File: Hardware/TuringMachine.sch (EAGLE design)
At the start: 78 parts, among them IC1 TL072P, IC2 4015, IC3 4015, IC5 4016, IC6 TL072P, IC7 TL072P, T1 2N3904

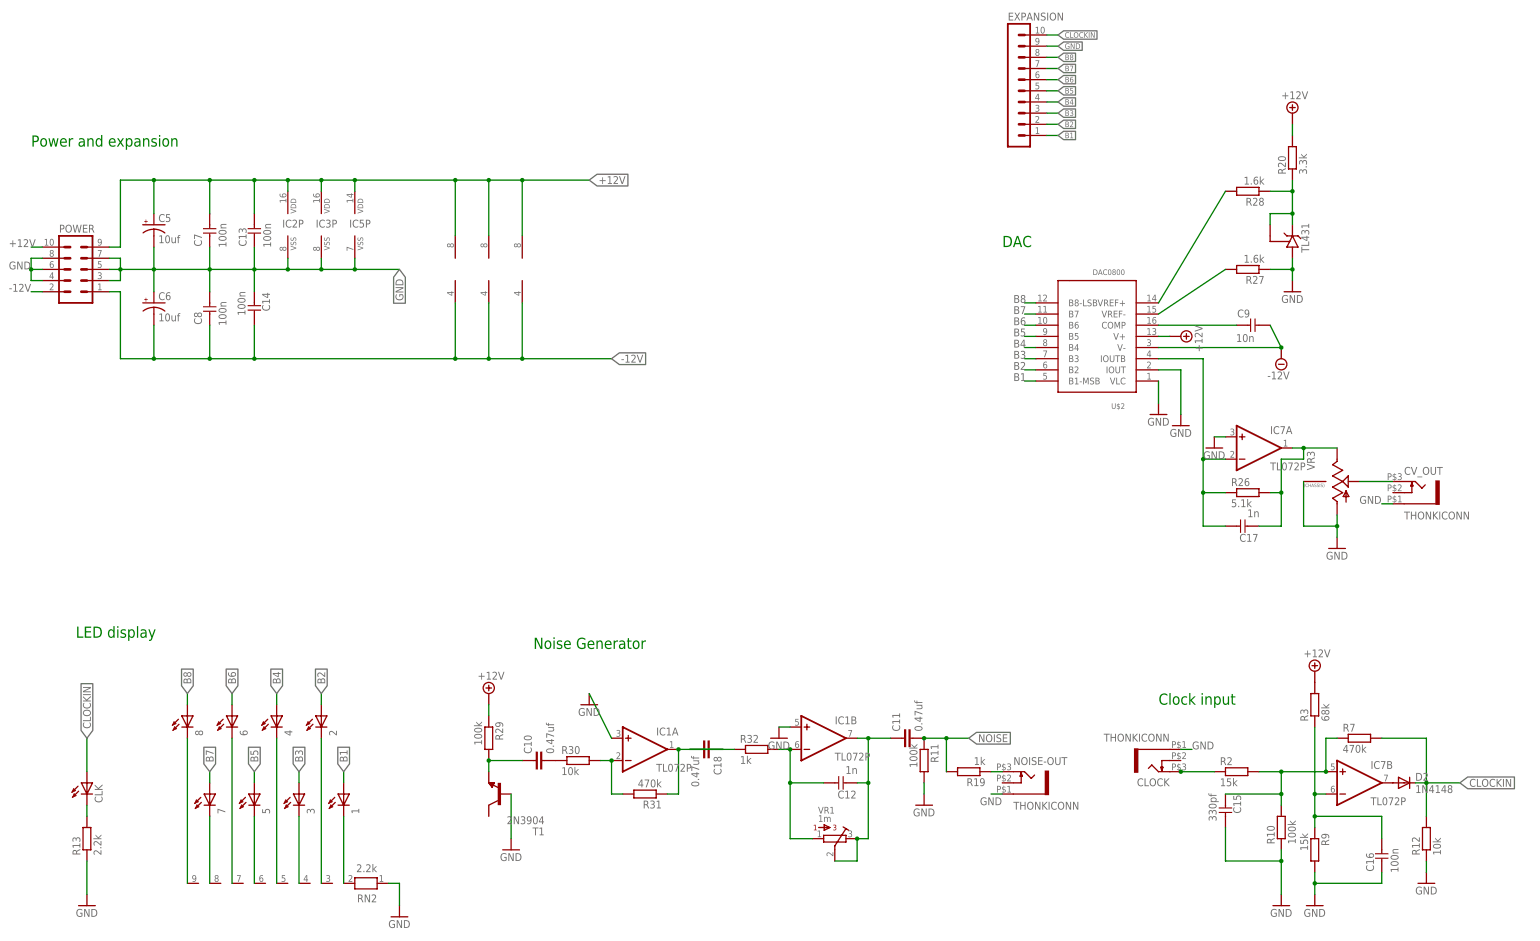
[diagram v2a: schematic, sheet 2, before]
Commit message: Fixes #5, fixes #4
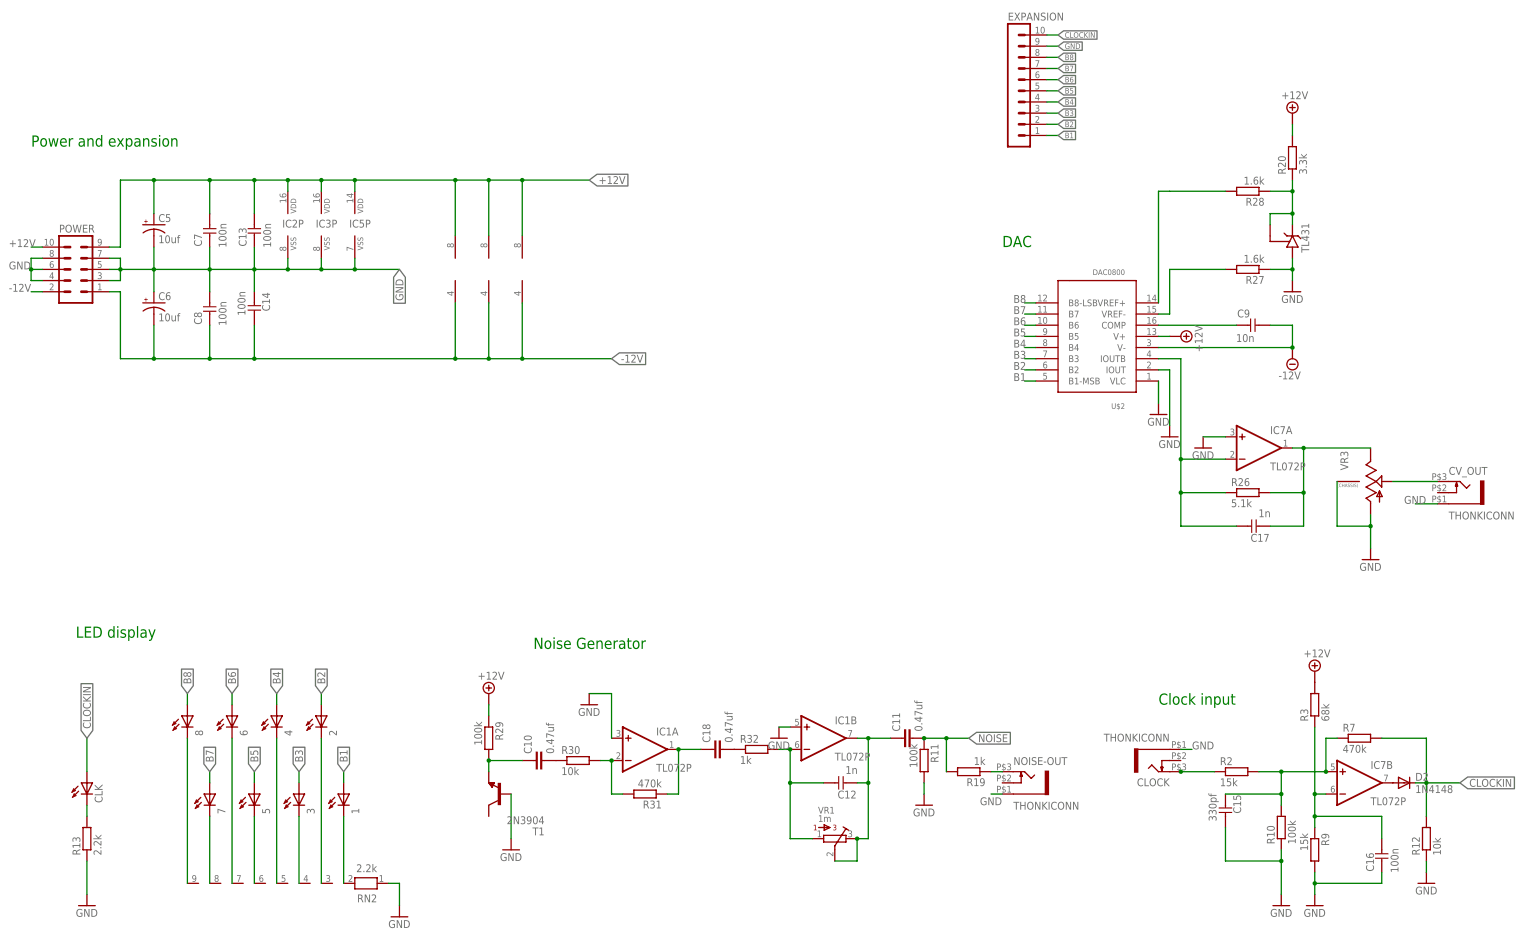
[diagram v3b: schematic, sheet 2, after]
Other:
- moved on the sheet: C17, C18, CV_OUT, VR3
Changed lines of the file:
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@@
 <instance part="U$2" gate="G$1" x="281.94" y="175.26" rot="R180"/>
 <instance part="SUPPLY7" gate="+12V" x="299.72" y="175.26" rot="R270"/>
-<instance part="SUPPLY8" gate="G$1" x="322.58" y="170.18"/>
-<instance part="GND23" gate="1" x="299.72" y="154.94"/>
+<instance part="SUPPLY8" gate="G$1" x="325.12" y="170.18"/>
+<instance part="GND23" gate="1" x="297.18" y="152.4"/>
 <instance part="R26" gate="G$1" x="314.96" y="139.7"/>
 <instance part="R27" gate="G$1" x="314.96" y="190.5" rot="R180"/>
@@
 <instance part="C9" gate="G$1" x="317.5" y="177.8" rot="R270"/>
 <instance part="IC7" gate="A" x="317.5" y="149.86"/>
-<instance part="GND18" gate="1" x="307.34" y="149.86"/>
-<instance part="GND19" gate="1" x="335.28" y="127"/>
-<instance part="CV_OUT" gate="G$1" x="353.06" y="139.7"/>
+<instance part="GND18" gate="1" x="304.8" y="149.86"/>
+<instance part="GND19" gate="1" x="342.9" y="124.46"/>
+<instance part="CV_OUT" gate="G$1" x="363.22" y="139.7"/>
 <instance part="GND5" gate="1" x="325.12" y="185.42"/>
 <instance part="IC1" gate="B" x="218.44" y="83.82"/>
@@
 <instance part="GND33" gate="1" x="50.8" y="45.72"/>
 <instance part="RN2" gate="1" x="114.3" y="50.8" rot="R180"/>
-<instance part="VR3" gate="G$1" x="335.28" y="142.24"/>
-<instance part="C17" gate="G$1" x="312.42" y="132.08" rot="R90"/>
+<instance part="VR3" gate="G$1" x="342.9" y="142.24"/>
+<instance part="C17" gate="G$1" x="314.96" y="132.08" rot="R90"/>
 <instance part="TL431" gate="G$1" x="325.12" y="198.12" rot="R90"/>
 <instance part="R20" gate="G$1" x="325.12" y="215.9" rot="R90"/>
-<instance part="C18" gate="G$1" x="193.04" y="81.28" rot="R270"/>
+<instance part="C18" gate="G$1" x="193.04" y="81.28" rot="R90"/>
 <instance part="IC1" gate="P" x="134.62" y="190.5"/>
 <instance part="IC7" gate="P" x="142.24" y="190.5"/>
@@
 <pinref part="U$2" gate="G$1" pin="V-"/>
 <pinref part="SUPPLY8" gate="G$1" pin="-12V"/>
-<wire x1="322.58" y1="172.72" x2="294.64" y2="172.72" width="0.1524" layer="91"/>
+<wire x1="325.12" y1="172.72" x2="294.64" y2="172.72" width="0.1524" layer="91"/>
 <pinref part="C9" gate="G$1" pin="1"/>
-<wire x1="320.04" y1="177.8" x2="322.58" y2="172.72" width="0.1524" layer="91"/>
-<junction x="322.58" y="172.72"/>
+<wire x1="320.04" y1="177.8" x2="325.12" y2="177.8" width="0.1524" layer="91"/>
+<wire x1="325.12" y1="177.8" x2="325.12" y2="172.72" width="0.1524" layer="91"/>
+<junction x="325.12" y="172.72"/>
 </segment>
 </net>
@@
 <segment>
 <pinref part="GND27" gate="1" pin="GND"/>
-<wire x1="165.1" y1="93.98" x2="170.18" y2="83.82" width="0.1524" layer="91"/>
+<wire x1="165.1" y1="93.98" x2="170.18" y2="93.98" width="0.1524" layer="91"/>
+<wire x1="170.18" y1="93.98" x2="170.18" y2="83.82" width="0.1524" layer="91"/>
 <pinref part="IC1" gate="A" pin="+IN"/>
 </segment>
@@
 <segment>
 <pinref part="U$2" gate="G$1" pin="IOUT"/>
-<wire x1="294.64" y1="167.64" x2="299.72" y2="167.64" width="0.1524" layer="91"/>
-<wire x1="299.72" y1="167.64" x2="299.72" y2="157.48" width="0.1524" layer="91"/>
+<wire x1="294.64" y1="167.64" x2="297.18" y2="167.64" width="0.1524" layer="91"/>
+<wire x1="297.18" y1="167.64" x2="297.18" y2="154.94" width="0.1524" layer="91"/>
 <pinref part="GND23" gate="1" pin="GND"/>
 </segment>
@@
 <pinref part="IC7" gate="A" pin="+IN"/>
 <pinref part="GND18" gate="1" pin="GND"/>
-<wire x1="309.88" y1="152.4" x2="307.34" y2="152.4" width="0.1524" layer="91"/>
+<wire x1="309.88" y1="152.4" x2="304.8" y2="152.4" width="0.1524" layer="91"/>
 </segment>
 <segment>
 <pinref part="CV_OUT" gate="G$1" pin="5"/>
-<wire x1="347.98" y1="137.16" x2="345.44" y2="137.16" width="0.1524" layer="91"/>
-<label x="340.36" y="137.16" size="1.778" layer="95"/>
+<wire x1="358.14" y1="137.16" x2="353.06" y2="137.16" width="0.1524" layer="91"/>
+<label x="350.52" y="137.16" size="1.778" layer="95"/>
 </segment>
 <segment>
@@
 <pinref part="GND19" gate="1" pin="GND"/>
 <pinref part="VR3" gate="G$1" pin="A"/>
-<wire x1="335.28" y1="129.54" x2="335.28" y2="132.08" width="0.1524" layer="91"/>
+<wire x1="342.9" y1="127" x2="342.9" y2="132.08" width="0.1524" layer="91"/>
 <pinref part="VR3" gate="G$1" pin="P$1"/>
-<wire x1="335.28" y1="132.08" x2="335.28" y2="134.62" width="0.1524" layer="91"/>
-<wire x1="327.66" y1="142.24" x2="327.66" y2="132.08" width="0.1524" layer="91"/>
-<wire x1="327.66" y1="132.08" x2="335.28" y2="132.08" width="0.1524" layer="91"/>
-<junction x="335.28" y="132.08"/>
+<wire x1="342.9" y1="132.08" x2="342.9" y2="134.62" width="0.1524" layer="91"/>
+<wire x1="335.28" y1="142.24" x2="335.28" y2="132.08" width="0.1524" layer="91"/>
+<wire x1="335.28" y1="132.08" x2="342.9" y2="132.08" width="0.1524" layer="91"/>
+<junction x="342.9" y="132.08"/>
 </segment>
 <segment>
@@
 <pinref part="IC1" gate="A" pin="OUT"/>
 <pinref part="C18" gate="G$1" pin="1"/>
-<wire x1="195.58" y1="81.28" x2="185.42" y2="81.28" width="0.1524" layer="91"/>
+<wire x1="190.5" y1="81.28" x2="185.42" y2="81.28" width="0.1524" layer="91"/>
 <junction x="185.42" y="81.28"/>
 </segment>
@@
 <segment>
 <pinref part="U$2" gate="G$1" pin="IOUTB"/>
-<wire x1="294.64" y1="170.18" x2="304.8" y2="170.18" width="0.1524" layer="91"/>
-<wire x1="304.8" y1="170.18" x2="304.8" y2="147.32" width="0.1524" layer="91"/>
-<wire x1="304.8" y1="147.32" x2="309.88" y2="147.32" width="0.1524" layer="91"/>
-<wire x1="304.8" y1="147.32" x2="304.8" y2="139.7" width="0.1524" layer="91"/>
-<junction x="304.8" y="147.32"/>
+<wire x1="294.64" y1="170.18" x2="299.72" y2="170.18" width="0.1524" layer="91"/>
+<wire x1="299.72" y1="170.18" x2="299.72" y2="147.32" width="0.1524" layer="91"/>
+<wire x1="299.72" y1="147.32" x2="309.88" y2="147.32" width="0.1524" layer="91"/>
+<wire x1="299.72" y1="147.32" x2="299.72" y2="139.7" width="0.1524" layer="91"/>
+<junction x="299.72" y="147.32"/>
 <pinref part="R26" gate="G$1" pin="1"/>
-<wire x1="304.8" y1="139.7" x2="309.88" y2="139.7" width="0.1524" layer="91"/>
+<wire x1="299.72" y1="139.7" x2="309.88" y2="139.7" width="0.1524" layer="91"/>
 <pinref part="IC7" gate="A" pin="-IN"/>
 <pinref part="C17" gate="G$1" pin="1"/>
-<wire x1="309.88" y1="132.08" x2="304.8" y2="132.08" width="0.1524" layer="91"/>
-<wire x1="304.8" y1="132.08" x2="304.8" y2="139.7" width="0.1524" layer="91"/>
-<junction x="304.8" y="139.7"/>
+<wire x1="312.42" y1="132.08" x2="299.72" y2="132.08" width="0.1524" layer="91"/>
+<wire x1="299.72" y1="132.08" x2="299.72" y2="139.7" width="0.1524" layer="91"/>
+<junction x="299.72" y="139.7"/>
 </segment>
 </net>
@@
 <wire x1="325.12" y1="149.86" x2="327.66" y2="149.86" width="0.1524" layer="91"/>
 <pinref part="VR3" gate="G$1" pin="E"/>
-<wire x1="327.66" y1="149.86" x2="335.28" y2="149.86" width="0.1524" layer="91"/>
-<wire x1="327.66" y1="149.86" x2="327.66" y2="147.32" width="0.1524" layer="91"/>
+<wire x1="327.66" y1="149.86" x2="342.9" y2="149.86" width="0.1524" layer="91"/>
 <junction x="327.66" y="149.86"/>
-<wire x1="327.66" y1="147.32" x2="322.58" y2="147.32" width="0.1524" layer="91"/>
-<wire x1="322.58" y1="147.32" x2="322.58" y2="139.7" width="0.1524" layer="91"/>
+<wire x1="327.66" y1="149.86" x2="327.66" y2="139.7" width="0.1524" layer="91"/>
 <pinref part="R26" gate="G$1" pin="2"/>
-<wire x1="322.58" y1="139.7" x2="320.04" y2="139.7" width="0.1524" layer="91"/>
+<wire x1="327.66" y1="139.7" x2="320.04" y2="139.7" width="0.1524" layer="91"/>
 <pinref part="C17" gate="G$1" pin="2"/>
-<wire x1="317.5" y1="132.08" x2="322.58" y2="132.08" width="0.1524" layer="91"/>
-<wire x1="322.58" y1="132.08" x2="322.58" y2="139.7" width="0.1524" layer="91"/>
-<junction x="322.58" y="139.7"/>
+<wire x1="320.04" y1="132.08" x2="327.66" y2="132.08" width="0.1524" layer="91"/>
+<wire x1="327.66" y1="132.08" x2="327.66" y2="139.7" width="0.1524" layer="91"/>
+<junction x="327.66" y="139.7"/>
 </segment>
 </net>
@@
 <pinref part="U$2" gate="G$1" pin="VREF+"/>
 <pinref part="R28" gate="G$1" pin="2"/>
-<wire x1="309.88" y1="208.28" x2="294.64" y2="182.88" width="0.1524" layer="91"/>
+<wire x1="309.88" y1="208.28" x2="297.18" y2="208.28" width="0.1524" layer="91"/>
+<wire x1="297.18" y1="208.28" x2="294.64" y2="208.28" width="0.1524" layer="91"/>
+<wire x1="294.64" y1="208.28" x2="294.64" y2="182.88" width="0.1524" layer="91"/>
 </segment>
 </net>
@@
 <pinref part="R27" gate="G$1" pin="2"/>
 <pinref part="U$2" gate="G$1" pin="VREF-"/>
-<wire x1="309.88" y1="190.5" x2="294.64" y2="180.34" width="0.1524" layer="91"/>
+<wire x1="309.88" y1="190.5" x2="297.18" y2="190.5" width="0.1524" layer="91"/>
+<wire x1="297.18" y1="190.5" x2="297.18" y2="180.34" width="0.1524" layer="91"/>
+<wire x1="297.18" y1="180.34" x2="294.64" y2="180.34" width="0.1524" layer="91"/>
 </segment>
 </net>
@@
 <segment>
 <pinref part="CV_OUT" gate="G$1" pin="3"/>
-<wire x1="340.36" y1="142.24" x2="347.98" y2="142.24" width="0.1524" layer="91"/>
+<wire x1="347.98" y1="142.24" x2="358.14" y2="142.24" width="0.1524" layer="91"/>
 <pinref part="VR3" gate="G$1" pin="S"/>
 </segment>
@@
 <pinref part="C18" gate="G$1" pin="2"/>
 <pinref part="R32" gate="G$1" pin="1"/>
-<wire x1="187.96" y1="81.28" x2="198.12" y2="81.28" width="0.1524" layer="91"/>
-</segment>
-</net>
+</segment>
+</net>

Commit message: not yet routed
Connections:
- net +12V: now also R1.2, R24.2; no longer R1.1, R24.1
- net N$4: now also R1.1; no longer R1.2
- net N$45: now also R24.1; no longer R24.2
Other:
- moved on the sheet: R1, R24
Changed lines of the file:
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@@
 <instance part="IC5" gate="B" x="193.04" y="111.76"/>
 <instance part="GND20" gate="1" x="172.72" y="86.36"/>
-<instance part="R24" gate="G$1" x="147.32" y="114.3" rot="R270"/>
+<instance part="R24" gate="G$1" x="147.32" y="114.3" rot="R90"/>
 <instance part="P+6" gate="+12V" x="147.32" y="121.92"/>
 <instance part="R22" gate="G$1" x="63.5" y="144.78" rot="R180"/>
@@
 <instance part="SUPPLY11" gate="G$1" x="58.42" y="134.62"/>
 <instance part="GND3" gate="1" x="172.72" y="149.86"/>
-<instance part="R1" gate="G$1" x="177.8" y="137.16" rot="R270"/>
+<instance part="R1" gate="G$1" x="177.8" y="137.16" rot="R90"/>
 <instance part="P+1" gate="+12V" x="177.8" y="147.32"/>
 <instance part="CV_IN" gate="G$1" x="45.72" y="121.92" rot="R180"/>
@@
 </segment>
 <segment>
-<pinref part="R24" gate="G$1" pin="1"/>
+<pinref part="R24" gate="G$1" pin="2"/>
 <pinref part="P+6" gate="+12V" pin="+12V"/>
 </segment>
@@
 </segment>
 <segment>
-<pinref part="R1" gate="G$1" pin="1"/>
+<pinref part="R1" gate="G$1" pin="2"/>
 <pinref part="P+1" gate="+12V" pin="+12V"/>
 <wire x1="177.8" y1="142.24" x2="177.8" y2="144.78" width="0.1524" layer="91"/>
@@
 <net name="N$45" class="0">
 <segment>
-<pinref part="R24" gate="G$1" pin="2"/>
+<pinref part="R24" gate="G$1" pin="1"/>
 <wire x1="147.32" y1="109.22" x2="147.32" y2="99.06" width="0.1524" layer="91"/>
 <wire x1="147.32" y1="109.22" x2="180.34" y2="109.22" width="0.1524" layer="91"/>
@@
 <net name="N$4" class="0">
 <segment>
-<pinref part="R1" gate="G$1" pin="2"/>
+<pinref part="R1" gate="G$1" pin="1"/>
 <wire x1="177.8" y1="132.08" x2="177.8" y2="129.54" width="0.1524" layer="91"/>
 <pinref part="IC5" gate="B" pin="A"/>

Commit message: throwing smd parts on the board
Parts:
- removed EXPANSION: (no value), TomW:MA10-1
- removed POWER: (no value), TomW:10_PIN_HEADER
- added 9, FUSE: FUSE, TomW:PTC_FUSEPOLY_FUSE
- added D1, D3: 1N4001, SparkFun-DiscreteSemi:DIODEHV
- added GATES, PULSES: (no value), con-lstb:MA08-2
- added IC10, IC9: 4050, 40xx:4050D
- added IC11, IC12: 78L09, linear:7808L
- added IC4, IC8: 4081, 40xx:4081D
- added POWER1: (no value), TomW:10_PIN_HEADER
- C1, C12, C13, C14, C15, C16, C17, C2, C4, C7, C8, C9: device TomW:C-EU050-024X044 -> SparkFun-Capacitors:CAP0805
- C10, C11, C18: device rcl:C-EU050-035X075 -> SparkFun-Capacitors:CAP0805
- C5, C6: device SparkFun-Passives:CAP_POLPTH2 -> SparkFun-Capacitors:CAP_POL1206
- D2: value 1N4148 -> BAT20JFILM; device MusicThingModular:SMALL_DIODEDO35-7 -> SparkFun-DiscreteSemi:BAT20JFILM
- IC1, IC6, IC7: value TL072P -> TL072_SMD; device TomW:TL072P -> MusicThingModular:TL072_SMD
- IC2, IC3: device 40xx:4015N -> 40xx:4015D
- IC5: device 40xx:4016N -> 40xx:4016D
- R1, R10, R12, R13, R14, R15, R16, R18, R19, R2, R20, R22, R23, R24, R26, R27, R28, R29, R3, R30, R31, R32, R35, R5, R6, R7, R8, R9: device TomW:R-EU_0207/7 -> SparkFun-Resistors:RESISTOR0805-RES
- R11: device MusicThingModular:RESISTOR6MM -> SparkFun-Resistors:RESISTOR0805-RES
- T1: value 2N3904 -> (none); device transistor:2N3904 -> transistor:MMBT3904LT1-NPN-SOT23-BEC
- U$2: value DAC0800 -> DAC0800SOIC; device TomW:DAC0800 -> TomW:DAC0800SOIC
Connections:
- new net CLOCK: GATES.10, GATES.9, IC10C.O, IC4C.I1, IC8A.I1, IC8B.I1, IC8C.I0, IC8D.I1, PULSES.10, PULSES.9
- new net CLOCK2: IC10D.O, IC4A.I1, IC4B.I1, IC4D.I1
- new net GATE1: GATES.1, IC10F.O
- new net GATE2: GATES.2, IC10E.O
- new net GATE3: GATES.3, IC10A.O
- new net GATE4: GATES.4, IC10B.O
- new net GATE5: GATES.5, IC9E.O
- new net GATE6: GATES.6, IC9D.O
- new net GATE7: GATES.7, IC9C.O
- new net GATE8: GATES.8, IC9A.O
- new net N$17: 9.P$2, POWER1.10, POWER1.9
- new net N$19: FUSE.P$2, POWER1.1, POWER1.2
- new net N$29: IC10P.VDD, IC11.VO
- new net N$38: IC12.VO, IC9P.VDD
- new net PULSE1: IC8D.O, PULSES.1
- new net PULSE2: IC8C.O, PULSES.2
- new net PULSE3: IC8A.O, PULSES.3
- new net PULSE4: IC8B.O, PULSES.4
- new net PULSE5: IC4D.O, PULSES.5
- new net PULSE6: IC4C.O, PULSES.6
- new net PULSE7: IC4B.O, PULSES.7
- new net PULSE8: IC4A.O, PULSES.8
- net +12V: now also 9.P$1, D1.C, GATES.15, GATES.16, IC11.VI, IC12.VI, IC4P.VDD, IC8P.VDD, PULSES.15, PULSES.16; no longer POWER.10, POWER.9
- net -12V: now also D3.A, FUSE.P$1, GATES.11, GATES.12, PULSES.11, PULSES.12; no longer POWER.1, POWER.2
- net B1: now also IC10F.I, IC8D.I0; no longer EXPANSION.1
- net B2: now also IC10E.I, IC8C.I1; no longer EXPANSION.2
- net B3: now also IC10A.I, IC8A.I0; no longer EXPANSION.3
- net B4: now also IC10B.I, IC8B.I0; no longer EXPANSION.4
- net B5: now also IC4D.I0, IC9E.I; no longer EXPANSION.5
- net B6: now also IC4C.I0, IC9D.I; no longer EXPANSION.6
- net B7: now also IC4B.I0, IC9C.I; no longer EXPANSION.7
- net B8: now also IC4A.I0, IC9A.I; no longer EXPANSION.8
- net CLOCKIN: now also IC10C.I, IC10D.I; no longer EXPANSION.10
- net GND: now also D1.A, D3.C, GATES.13, GATES.14, IC10P.VSS, IC11.GND, IC12.GND, IC4P.VSS, IC8P.VSS, IC9B.I, IC9F.I, IC9P.VSS, POWER1.3, POWER1.4, POWER1.5, POWER1.6, POWER1.7, POWER1.8, PULSES.13, PULSES.14; no longer EXPANSION.9, POWER.3, POWER.4, POWER.5, POWER.6, POWER.7, POWER.8
